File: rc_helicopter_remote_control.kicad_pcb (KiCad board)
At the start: 2 copper layers, 39 parts, among them J1 SWD, SW1 SW_SPST, U1 STM32L4P5RET6, U2 LTC3440EMS, U3 NRF24L01_Breakout, Y1 16MHz

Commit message: Improve DCDC converter diagram
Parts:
- U2: footprint Local_Library:SOP50P490X110-10N -> Package_SO:MSOP-10_3x3mm_P0.5mm
- moved JOY2 91.8 mm to (159.9, 38.9)
- renumbered C9 to C8, C8 to C9, R6 to R5, R5 to R6
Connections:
- net +BATT renamed /Power/+BATT
- net /Power/FB renamed Net-(U2-Pad9)
- R6 pad 1: Net-(R5-Pad1) -> GND
- R6 pad 2: GND -> Net-(U2-Pad1)
- U2 pad 1: Net-(R5-Pad1) -> Net-(U2-Pad1)

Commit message: Arrange footprints
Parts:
- removed BT1: Li-Ion, Local_Library:BAT_BCAAAW
- removed R12, R13, R14, R15: 100Ω, Resistor_SMD:R_0603_1608Metric
- added D4: Blue, LED_SMD:LED_0603_1608Metric, F.Cu at (143.2, 118.3)
- added D5: Blue, LED_SMD:LED_0603_1608Metric, F.Cu at (140.2, 118.3)
- added J2: SWD, Connector_PinHeader_2.54mm:PinHeader_1x06_P2.54mm_Vertical_SMD_Pin1Left, F.Cu at (163.1, 103.3)
- added REF**: MountingHole_3mm_Pad_Via, MountingHole:MountingHole_3mm_Pad_Via, F.Cu at (191.0, 80.0)
- added REF**: MountingHole_3mm_Pad_Via, MountingHole:MountingHole_3mm_Pad_Via, F.Cu at (101.0, 80.0)
- added REF**: MountingHole_3mm_Pad_Via, MountingHole:MountingHole_3mm_Pad_Via, F.Cu at (101.0, 120.0)
- added REF**: MountingHole_3mm_Pad_Via, MountingHole:MountingHole_3mm_Pad_Via, F.Cu at (191.0, 120.0)
- added RV1: 100kΩ, Potentiometer_THT:Potentiometer_ACP_CA14V-15_Vertical, F.Cu at (156.4, 76.9)
- added RV2: 100kΩ, Potentiometer_THT:Potentiometer_ACP_CA14V-15_Vertical, F.Cu at (125.8, 76.9)
- added SW2: SW_Push, Button_Switch_THT:SW_PUSH_6mm_H13mm, F.Cu at (107.2, 118.0)
- added SW3: SW_Push, Button_Switch_THT:SW_PUSH_6mm_H13mm, F.Cu at (121.2, 115.0)
- added SW4: SW_Push, Button_Switch_THT:SW_PUSH_6mm_H13mm, F.Cu at (164.2, 115.0)
- added SW5: SW_Push, Button_Switch_THT:SW_PUSH_6mm_H13mm, F.Cu at (177.8, 118.0)
- D1, D2, D3: value LED_RGBK -> Blue; footprint LED_SMD:LED_Avago_PLCC4_3.2x2.8mm_CW -> LED_SMD:LED_0603_1608Metric
- J1: value SWD -> Battery Pack; footprint Connector_PinHeader_2.54mm:PinHeader_2x03_P2.54mm_Vertical -> Connector_Molex:Molex_KK-254_AE-6410-02A_1x02_P2.54mm_Vertical
- R10, R11: value 100Ω -> 140Ω
- R7, R8, R9: value 180Ω -> 140Ω
- SW1: footprint Button_Switch_SMD:SW_DIP_SPSTx01_Slide_9.78x4.72mm_W8.61mm_P2.54mm -> Button_Switch_THT:SW_Slide_1P2T_CK_OS102011MS2Q
- moved R1 85.0 mm to (157.8, 109.6)
- moved R4 75.2 mm to (136.9, 96.0), turned to 90 degrees
- moved C7 72.5 mm to (148.5, 95.7)
- moved R2 71.7 mm to (151.6, 95.7), turned to 180 degrees
- moved R3 70.0 mm to (137.6, 98.3)
- moved R6 69.9 mm to (131.2, 94.6), turned to 180 degrees
- moved U2 67.0 mm to (132.8, 97.3)
- moved C6 66.2 mm to (158.8, 100.7), turned to -90 degrees
- moved C9 64.7 mm to (134.5, 94.6)
- moved JOY2 64.7 mm to (181.0, 100.0)
- moved C10 62.9 mm to (136.0, 104.1), turned to -90 degrees
- moved C1 58.3 mm to (142.7, 99.4)
- moved C5 56.0 mm to (153.8, 111.1), turned to 180 degrees
- moved C3 53.8 mm to (142.7, 106.8)
- moved SW1 52.7 mm to (115.6, 80.1)
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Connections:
- C8 pad 1: GND -> +3.3V
- C8 pad 2: +3.3V -> GND
- D1 pad 1: Net-(D1-Pad1) -> GND
- D2 pad 1: Net-(D2-Pad1) -> GND
- D3 pad 1: Net-(D3-Pad1) -> GND
- J1 pad 1: +3.3V -> +BATT
- J1 pad 2: /SWCLK -> GND
- JOY2 pad 2: /JOY1_Y -> /JOY2_Y
- JOY2 pad 5: /JOY1_X -> /JOY2_X
- JOY2 pad 7: /JOY1_S -> /JOY2_S
- R10 pad 1: Net-(D1-Pad2) -> /LED4
- R10 pad 2: /LED1_G -> Net-(D4-Pad2)
- R11 pad 1: Net-(D2-Pad2) -> /LED5
- R11 pad 2: /LED2_G -> Net-(D5-Pad2)
- R7 pad 1: Net-(D1-Pad1) -> /LED1
- R7 pad 2: /LED1_R -> Net-(D1-Pad2)
- R8 pad 1: Net-(D2-Pad1) -> /LED2
- R8 pad 2: /LED2_R -> Net-(D2-Pad2)
- R9 pad 1: Net-(D3-Pad1) -> /LED3
- R9 pad 2: /LED3_R -> Net-(D3-Pad2)
- SW1 pad 1: /Power/+BATT -> Net-(C10-Pad1)
- SW1 pad 2: Net-(C10-Pad1) -> +BATT
- U1 pad 29: /LED2_R -> unconnected-(U1-Pad29)
- U1 pad 30: /LED2_G -> /LED1
- U1 pad 33: /LED2_B -> /LED2
- U1 pad 34: /LED3_R -> /LED3
- U1 pad 35: /LED3_G -> /LED4
- U1 pad 36: /LED3_B -> /LED5
- U1 pad 45: unconnected-(U1-Pad45) -> /POT1
- U1 pad 50: unconnected-(U1-Pad50) -> /POT2
- U1 pad 58: unconnected-(U1-Pad58) -> /SW1
- U1 pad 59: /LED1_R -> /SW2
- U1 pad 61: /LED1_G -> /SW3
- U1 pad 62: /LED1_B -> /SW4
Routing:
- added copper zone on B.Cu, net +3.3V
- added copper zone on F.Cu, net GND
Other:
- board outline added: 100 x 50 mm

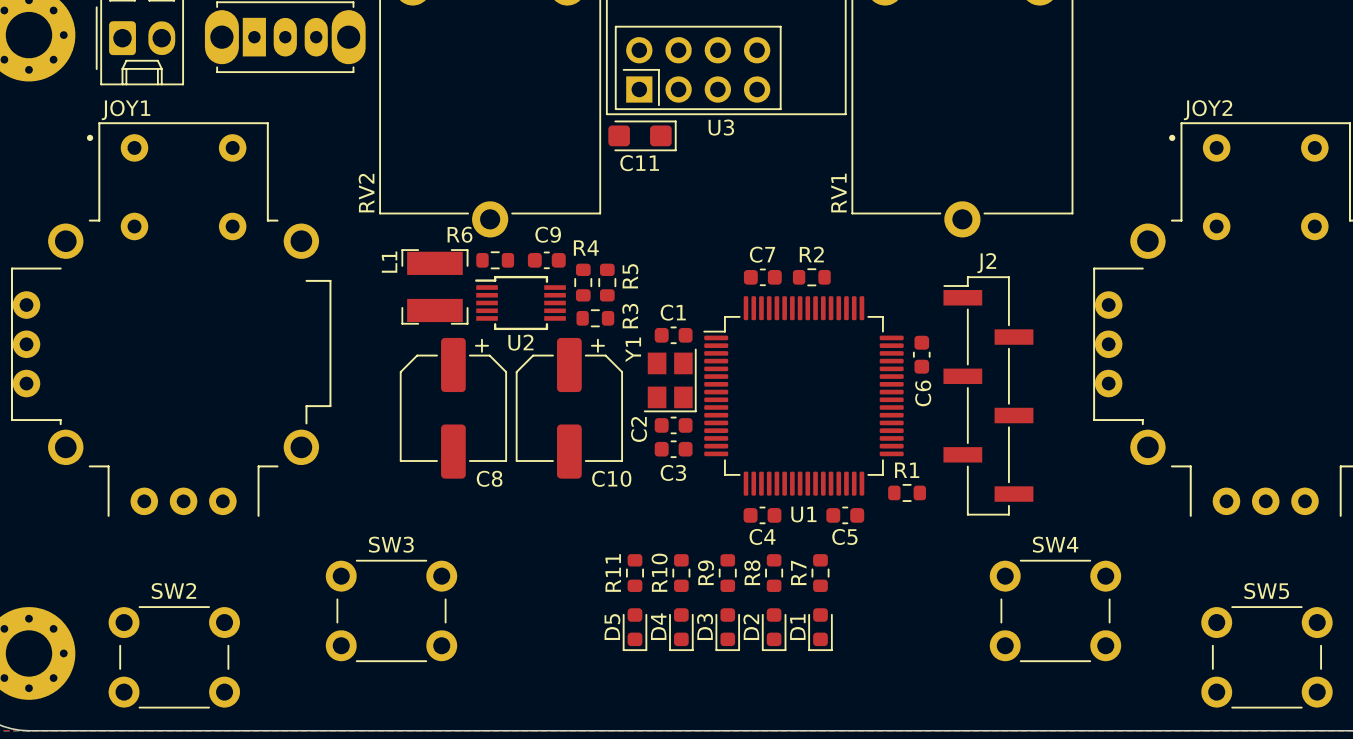
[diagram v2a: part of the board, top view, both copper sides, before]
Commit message: Use more appropriate MCU pins for peripherals
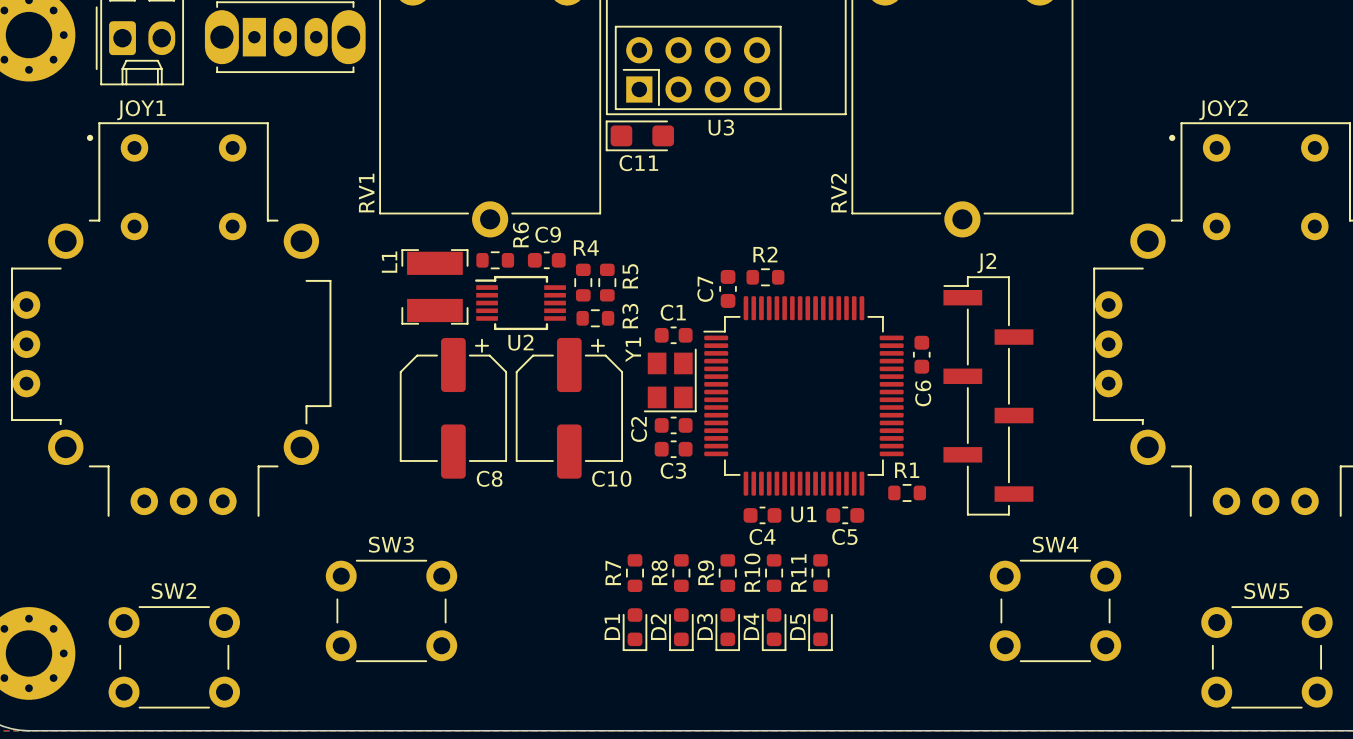
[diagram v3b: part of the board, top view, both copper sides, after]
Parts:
- moved R2 3.00 mm to (148.6, 95.7), turned to 0 degrees
- moved C7 2.37 mm to (146.2, 96.4), turned to 90 degrees
- moved C11 0.15 mm to (140.7, 86.5), turned to 0 degrees
- turned C3 to 180 degrees
- renumbered D5 to D1, D4 to D2, D2 to D4, D1 to D5, R8 to R10, R7 to R11, R11 to R7, R10 to R8, RV2 to RV1, RV1 to RV2
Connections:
- J2 pad 6: /SWO -> unconnected-(J2-Pad6)
- R10 pad 1: /LED2 -> /LED4
- R11 pad 1: /LED1 -> /LED5
- R7 pad 1: /LED5 -> /LED1
- R8 pad 1: /LED4 -> /LED2
- RV1 pad 2: /POT2 -> /POT1
- RV2 pad 2: /POT1 -> /POT2
- SW1 pad 1: Net-(C10-Pad1) -> unconnected-(SW1-Pad1)
- SW1 pad 3: unconnected-(SW1-Pad3) -> Net-(C10-Pad1)
- SW2 pad 1: GND -> /SW1
- SW2 pad 2: /SW1 -> GND
- SW3 pad 1: GND -> /SW2
- SW3 pad 2: /SW2 -> GND
- SW4 pad 1: GND -> /SW3
- SW4 pad 2: /SW3 -> GND
- SW5 pad 1: GND -> /SW4
- SW5 pad 2: /SW4 -> GND
- U1 pad 14: /JOY1_Y -> /JOY1_S
- U1 pad 15: /JOY1_X -> /JOY1_Y
- U1 pad 16: /JOY1_S -> /JOY1_X
- U1 pad 17: unconnected-(U1-Pad17) -> /SW2
- U1 pad 20: /NRF_CSN -> /SW1
- U1 pad 21: /NRF_SCK -> /LED1
- U1 pad 22: /NRF_MISO -> /LED2
- U1 pad 23: /NRF_MOSI -> /LED3
- U1 pad 24: unconnected-(U1-Pad24) -> /POT2
- U1 pad 25: unconnected-(U1-Pad25) -> /JOY2_X
- U1 pad 26: /NRF_CE -> /JOY2_Y
- U1 pad 27: unconnected-(U1-Pad27) -> /LED4
- U1 pad 28: unconnected-(U1-Pad28) -> /LED5
- U1 pad 30: /LED1 -> unconnected-(U1-Pad30)
- U1 pad 33: /LED2 -> /SW4
- U1 pad 34: /LED3 -> /SW3
- U1 pad 35: /LED4 -> unconnected-(U1-Pad35)
- U1 pad 36: /LED5 -> unconnected-(U1-Pad36)
- U1 pad 41: /NRF_IRQ -> unconnected-(U1-Pad41)
- U1 pad 42: /JOY2_Y -> unconnected-(U1-Pad42)
- U1 pad 43: /JOY2_X -> unconnected-(U1-Pad43)
- U1 pad 44: /JOY2_S -> unconnected-(U1-Pad44)
- U1 pad 45: /POT1 -> unconnected-(U1-Pad45)
- U1 pad 50: /POT2 -> /JOY2_S
- U1 pad 54: unconnected-(U1-Pad54) -> /NRF_IRQ
- U1 pad 55: /SWO -> /NRF_SCK
- U1 pad 56: unconnected-(U1-Pad56) -> /NRF_MISO
- U1 pad 57: unconnected-(U1-Pad57) -> /NRF_MOSI
- U1 pad 58: /SW1 -> /NRF_CSN
- U1 pad 59: /SW2 -> /NRF_CE
- U1 pad 61: /SW3 -> unconnected-(U1-Pad61)
- U1 pad 62: /SW4 -> unconnected-(U1-Pad62)
- U1 pad 8: unconnected-(U1-Pad8) -> /POT1

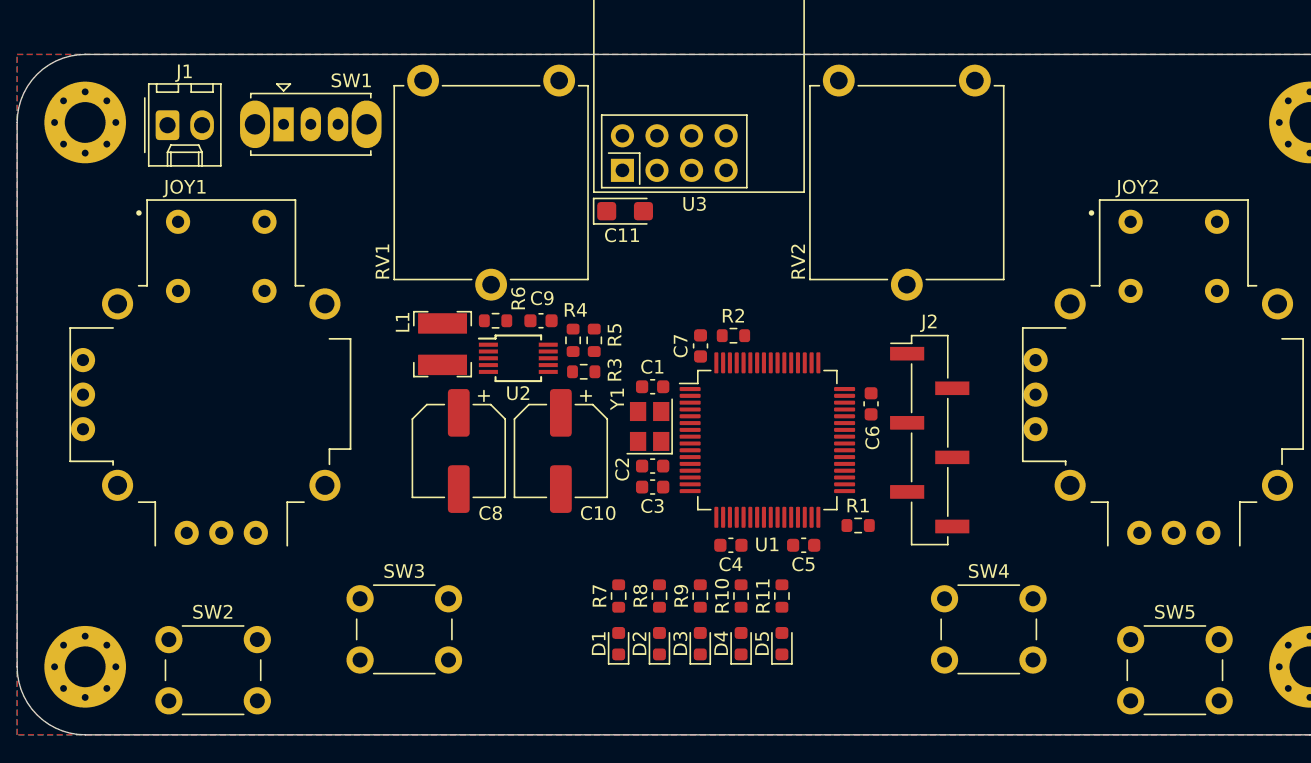
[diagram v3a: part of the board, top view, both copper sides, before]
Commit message: Route PCB tracks
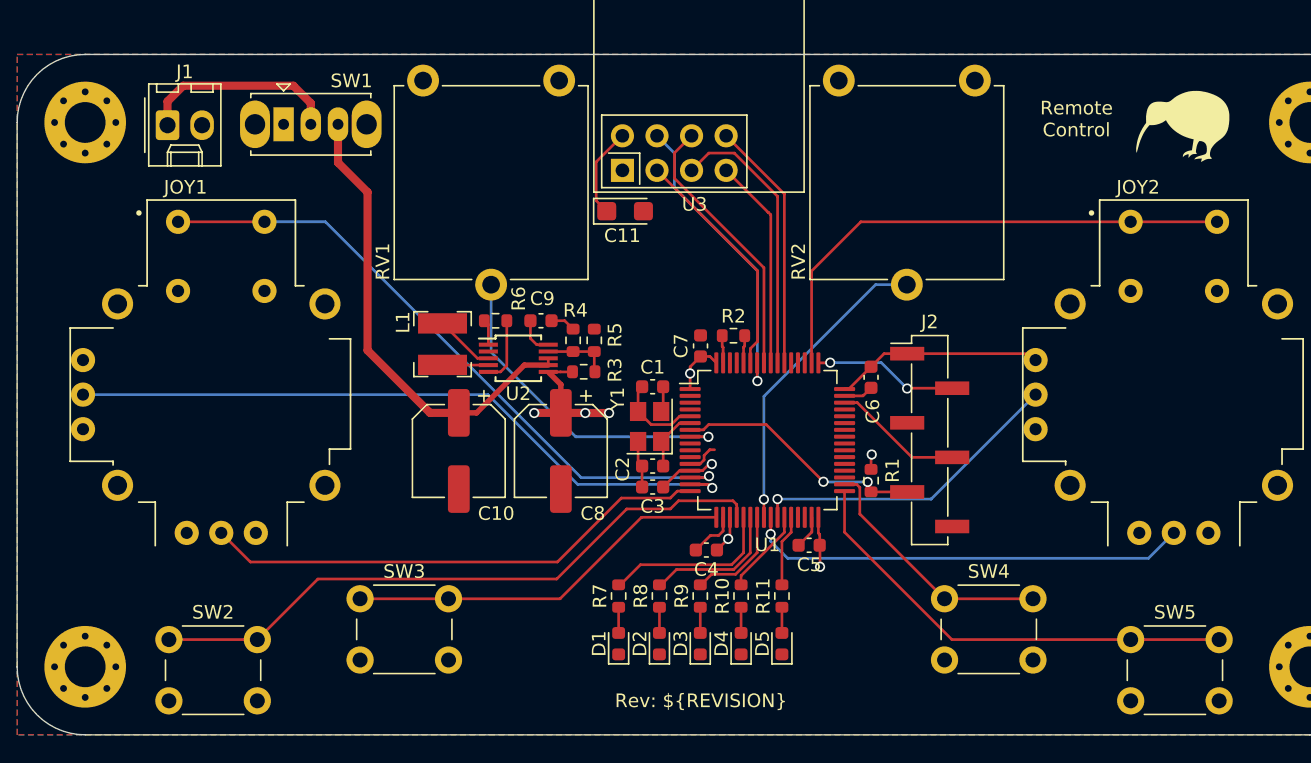
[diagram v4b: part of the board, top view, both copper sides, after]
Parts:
- added G***: LOGO, Local_Library:Kiwi, F.Cu at (181.7, 80.3)
- moved C10 7.50 mm to (128.5, 104.1)
- moved C8 7.50 mm to (136.0, 104.1)
- moved R1 3.43 mm to (158.8, 106.3), turned to -90 degrees
- moved C6 1.95 mm to (158.8, 98.7)
- moved C4 1.83 mm to (146.6, 111.4)
- moved C5 0.40 mm to (154.2, 111.1)
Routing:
- net /JOY1_Y: track 0.00 -> 50.8 mm, vias 0 -> 1
- net +3.3V: track 0.00 -> 48.5 mm, vias 0 -> 8
- net /JOY1_S: track 0.00 -> 48.3 mm, vias 0 -> 1
- net /SW1: track 0.00 -> 47.0 mm
- net /JOY2_S: track 0.00 -> 38.0 mm
- net /JOY1_X: track 0.00 -> 37.5 mm
- net Net-(C10-Pad1): track 0.00 -> 34.6 mm
- net /SW4: track 0.00 -> 33.8 mm
- net /JOY2_X: track 0.00 -> 32.7 mm, vias 0 -> 1
- net /SW2: track 0.00 -> 28.7 mm
- net /POT1: track 0.00 -> 24.9 mm, vias 0 -> 1
- net /JOY2_Y: track 0.00 -> 23.5 mm, vias 0 -> 1
- net GND: track 0.00 -> 22.9 mm
- net /POT2: track 0.00 -> 22.8 mm, vias 0 -> 1
- net /NRF_CSN: track 0.00 -> 22.4 mm, vias 0 -> 1
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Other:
- board text added: "Remote Control"
- board text added: "Rev: ${REVISION}"

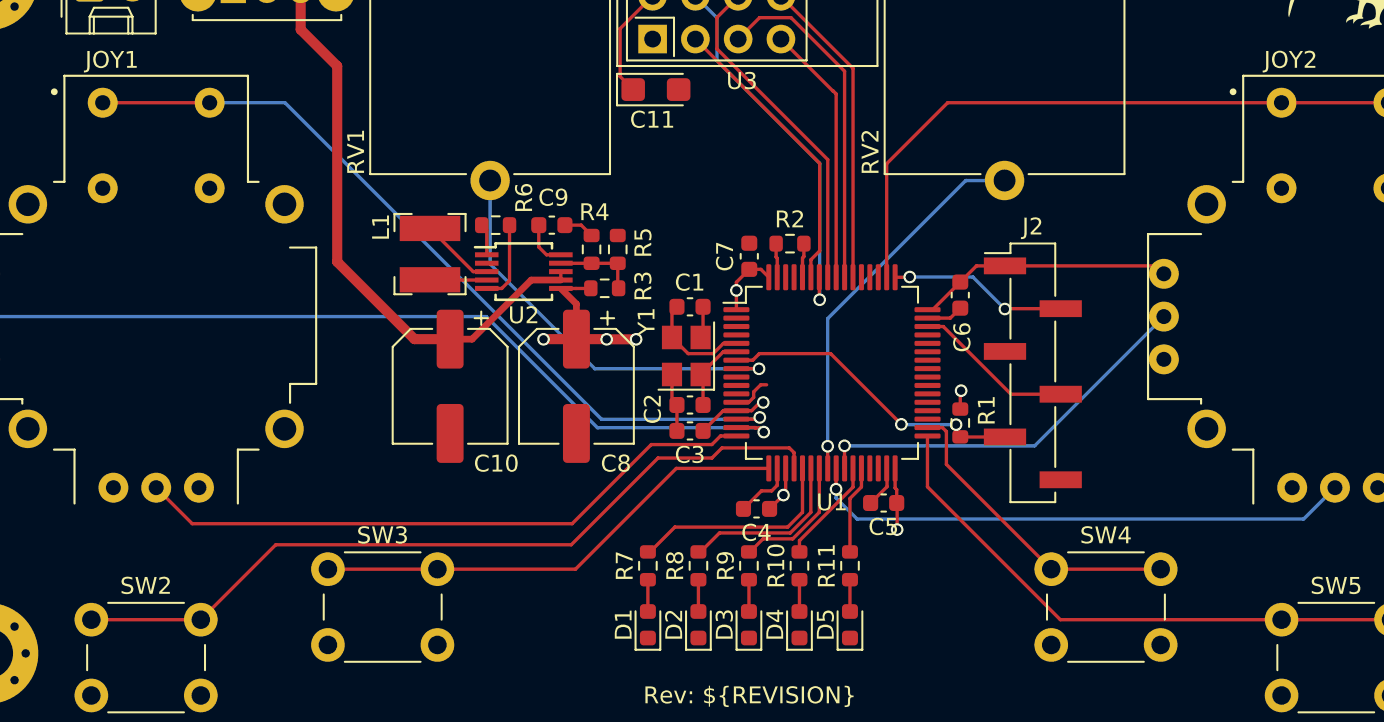
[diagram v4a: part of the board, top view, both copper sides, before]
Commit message: Improve the routing
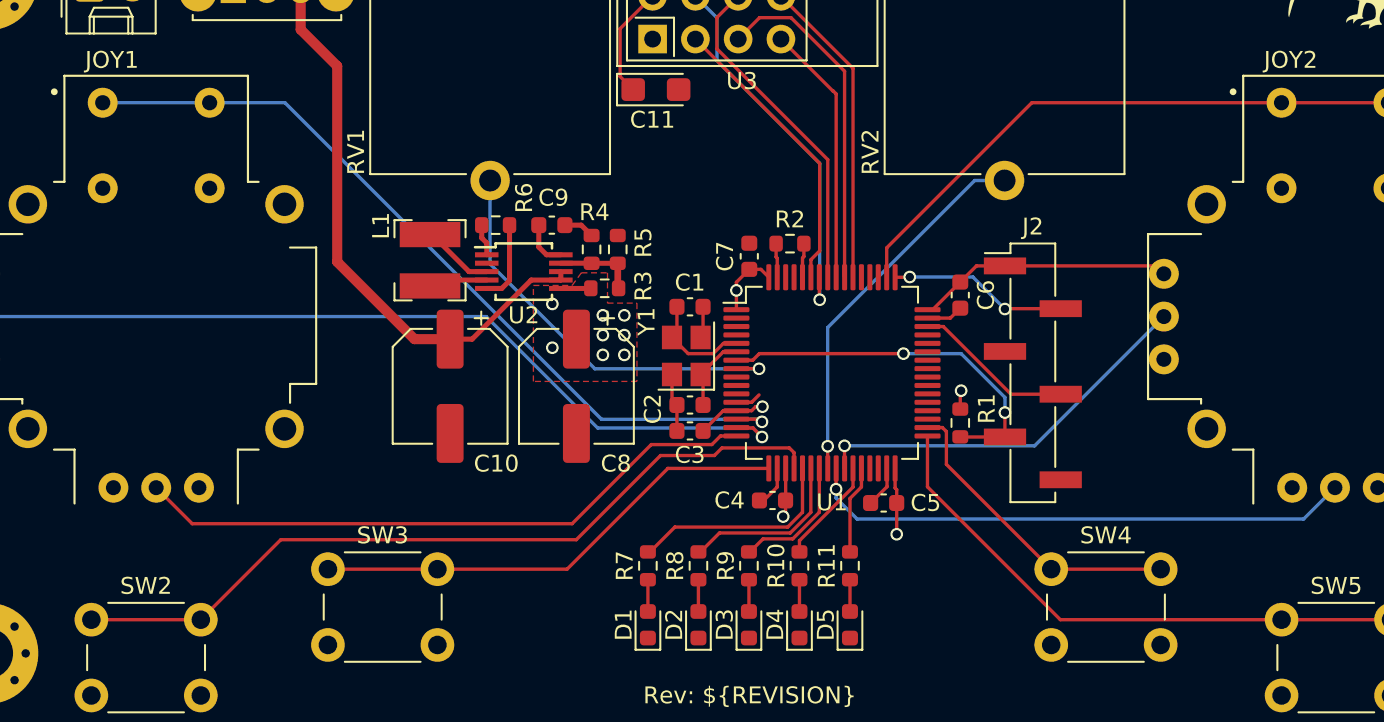
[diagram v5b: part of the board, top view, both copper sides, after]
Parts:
- moved C4 1.07 mm to (147.6, 110.9)
- moved L1 0.36 mm to (127.3, 96.7)
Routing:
- net +3.3V: track 48.5 -> 39.9 mm, vias 8 -> 13
- net /NRST: track 18.4 -> 22.2 mm
- net /JOY2_S: track 38.0 -> 35.1 mm
- net GND: track 22.9 -> 20.9 mm
- added copper zone on F.Cu, net +3.3V
